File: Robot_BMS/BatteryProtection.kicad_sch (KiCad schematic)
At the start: 18 parts, among them Q10 SIS413DN-T1-GE3, Q11 SIS413DN-T1-GE3, Q12 SIS413DN-T1-GE3, Q13 SIS413DN-T1-GE3, Q14 SIS413DN-T1-GE3, Q15 SIS413DN-T1-GE3, U7 BQ297xy, U8 BQ297xy, U9 BQ297xy

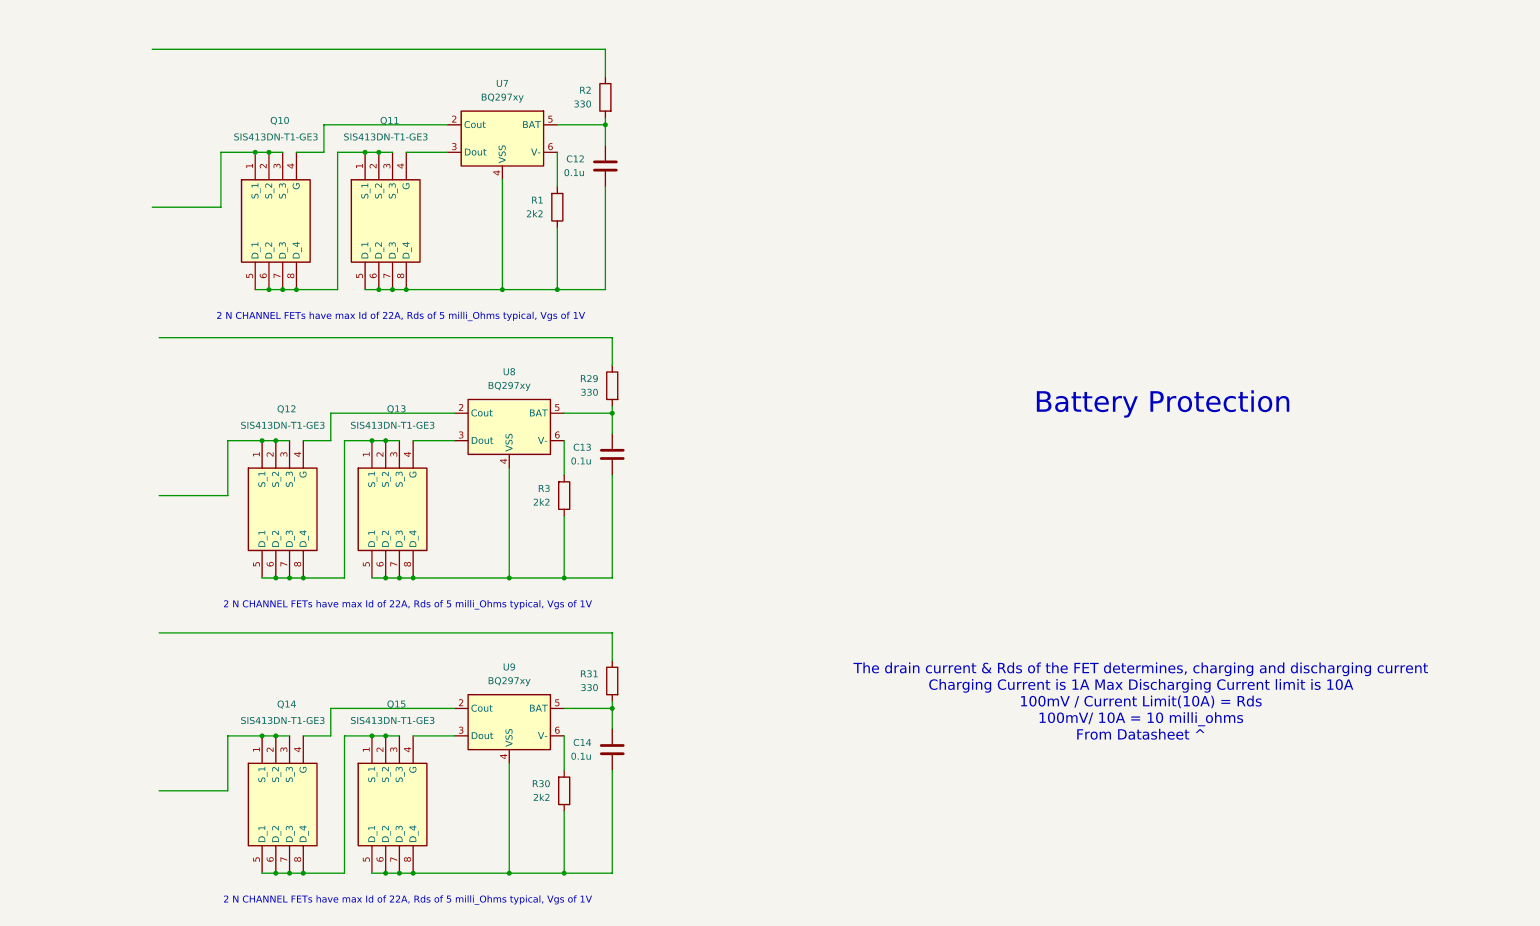
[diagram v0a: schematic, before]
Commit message: cleaning up hierarchical schematics
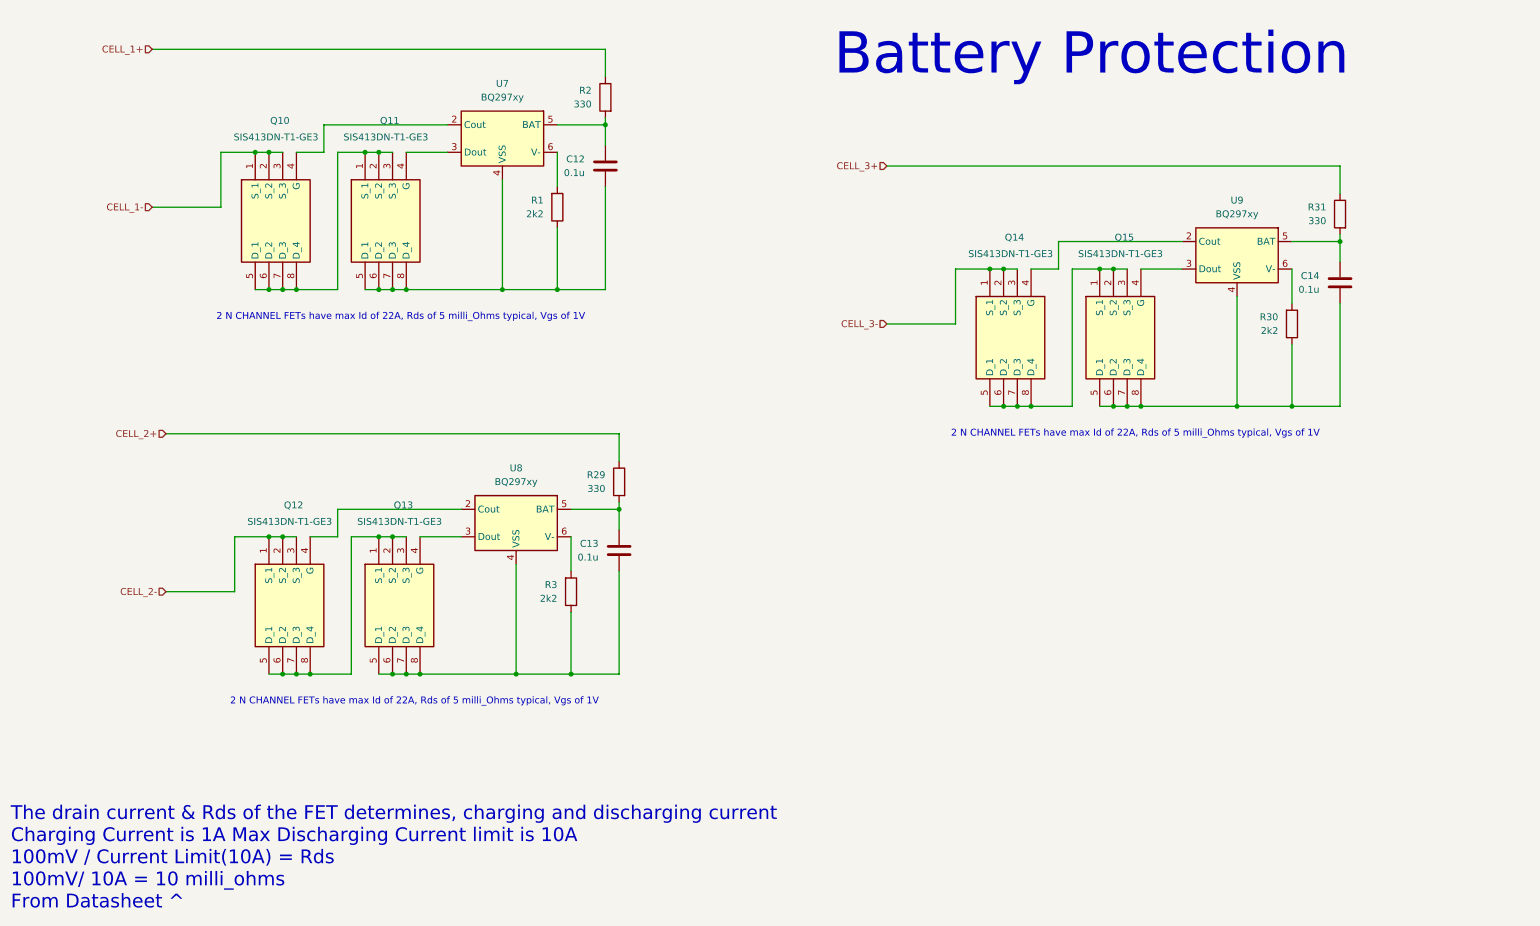
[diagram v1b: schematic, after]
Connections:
- net CELL_1+: now reaches R2.1
- net CELL_3-: now reaches Q14.1 (S_1), Q14.2 (S_2), Q14.3 (S_3)
- net CELL_1-: now reaches Q10.1 (S_1), Q10.2 (S_2), Q10.3 (S_3)
- net CELL_2-: now reaches Q12.1 (S_1), Q12.2 (S_2), Q12.3 (S_3)
- net CELL_2+: now reaches R29.1
- net CELL_3+: now reaches R31.1
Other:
- moved on the sheet: C13, C14, Q12, Q13, Q14, Q15, R29, R3, R30, R31, U8, U9

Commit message: DC power supply added via dc Barrel jack
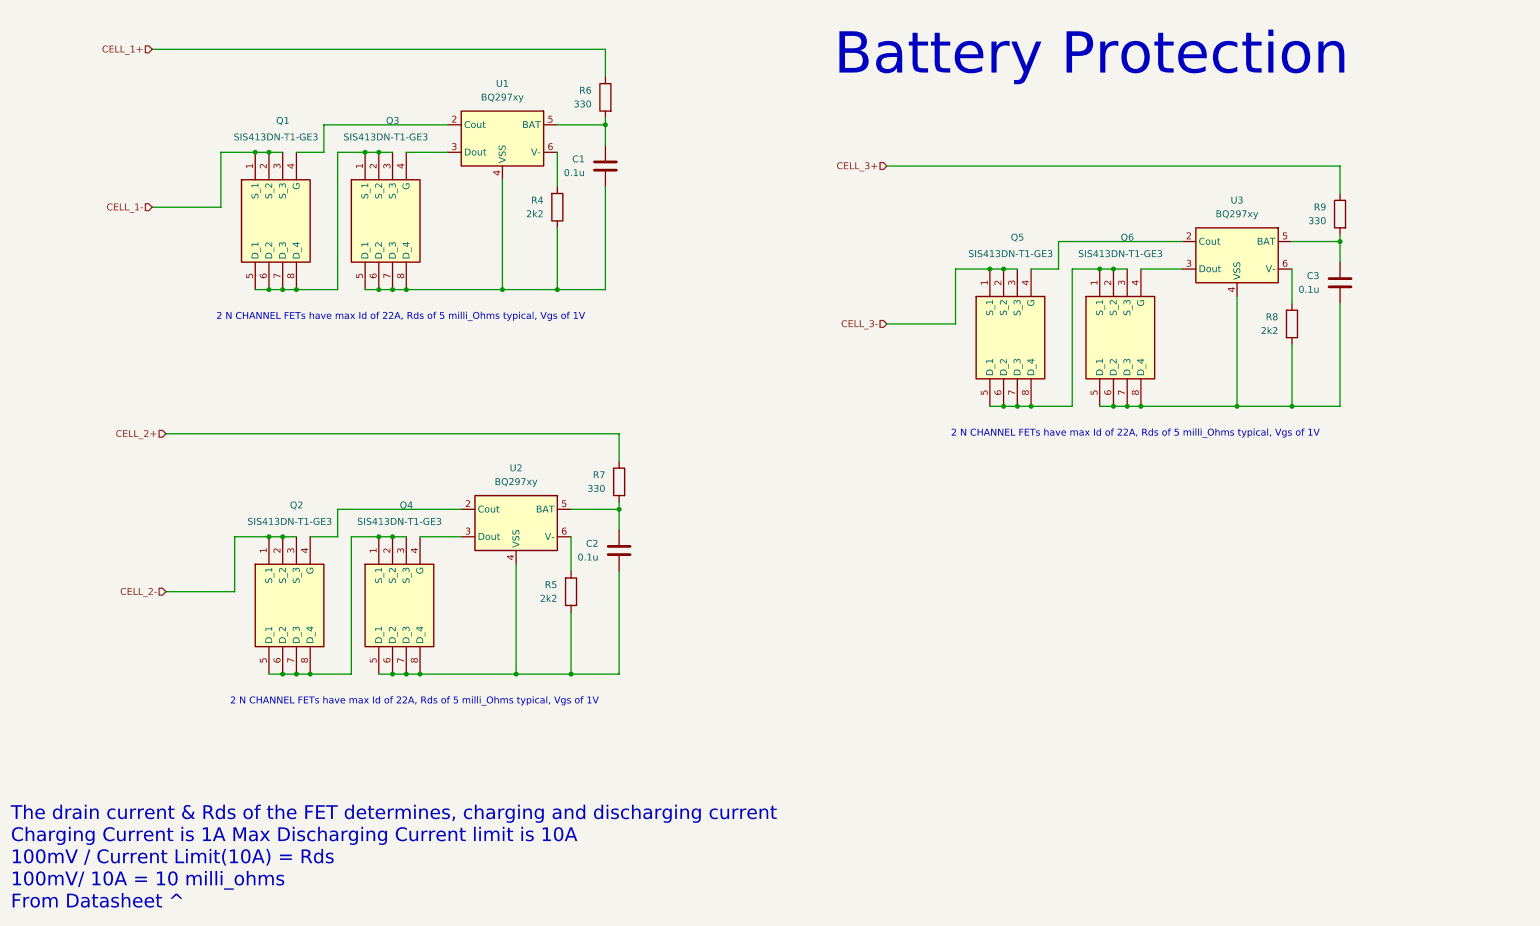
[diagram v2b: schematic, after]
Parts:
- renumbered C12 to C1, C13 to C2, C14 to C3, Q10 to Q1, Q12 to Q2, Q11 to Q3, Q13 to Q4, Q14 to Q5, Q15 to Q6, R1 to R4, R3 to R5, R2 to R6, R29 to R7, R30 to R8, R31 to R9, U7 to U1, U8 to U2, U9 to U3
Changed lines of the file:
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@@
 		(on_board yes)
 		(dnp no)
-		(property "Reference" "Q13"
+		(property "Reference" "Q4"
 			(at 87.63 113.538 90)
 			(effects
@@
 			(project "Robot_BMS"
 				(path "/72551b1c-3d40-4199-8911-e5b015f4abec/ba86123e-f6d5-4f01-be08-e30873977d47"
-					(reference "Q13")
+					(reference "Q4")
 					(unit 1)
 				)
@@
 		(dnp no)
 		(fields_autoplaced yes)
-		(property "Reference" "U9"
+		(property "Reference" "U3"
 			(at 240.03 57.15 0)
 			(effects
@@
 			(project "Robot_BMS"
 				(path "/72551b1c-3d40-4199-8911-e5b015f4abec/ba86123e-f6d5-4f01-be08-e30873977d47"
-					(reference "U9")
+					(reference "U3")
 					(unit 1)
 				)
@@
 		(dnp no)
 		(fields_autoplaced yes)
-		(property "Reference" "R1"
+		(property "Reference" "R4"
 			(at 111.76 57.1499 0)
 			(effects
@@
 			(project "Robot_BMS"
 				(path "/72551b1c-3d40-4199-8911-e5b015f4abec/ba86123e-f6d5-4f01-be08-e30873977d47"
-					(reference "R1")
+					(reference "R4")
 					(unit 1)
 				)
@@
 		(dnp no)
 		(fields_autoplaced yes)
-		(property "Reference" "R2"
+		(property "Reference" "R6"
 			(at 120.65 36.8299 0)
 			(effects
@@
 			(project "Robot_BMS"
 				(path "/72551b1c-3d40-4199-8911-e5b015f4abec/ba86123e-f6d5-4f01-be08-e30873977d47"
-					(reference "R2")
+					(reference "R6")
 					(unit 1)
 				)
@@
 		(on_board yes)
 		(dnp no)
-		(property "Reference" "Q14"
+		(property "Reference" "Q5"
 			(at 200.66 64.008 90)
 			(effects
@@
 			(project "Robot_BMS"
 				(path "/72551b1c-3d40-4199-8911-e5b015f4abec/ba86123e-f6d5-4f01-be08-e30873977d47"
-					(reference "Q14")
+					(reference "Q5")
 					(unit 1)
 				)
@@
 		(on_board yes)
 		(dnp no)
-		(property "Reference" "Q10"
+		(property "Reference" "Q1"
 			(at 64.77 42.418 90)
 			(effects
@@
 			(project "Robot_BMS"
 				(path "/72551b1c-3d40-4199-8911-e5b015f4abec/ba86123e-f6d5-4f01-be08-e30873977d47"
-					(reference "Q10")
+					(reference "Q1")
 					(unit 1)
 				)
@@
 		(dnp no)
 		(fields_autoplaced yes)
-		(property "Reference" "R3"
+		(property "Reference" "R5"
 			(at 114.3 128.2699 0)
 			(effects
@@
 			(project "Robot_BMS"
 				(path "/72551b1c-3d40-4199-8911-e5b015f4abec/ba86123e-f6d5-4f01-be08-e30873977d47"
-					(reference "R3")
+					(reference "R5")
 					(unit 1)
 				)
@@
 		(on_board yes)
 		(dnp no)
-		(property "Reference" "Q15"
+		(property "Reference" "Q6"
 			(at 220.98 64.008 90)
 			(effects
@@
 			(project "Robot_BMS"
 				(path "/72551b1c-3d40-4199-8911-e5b015f4abec/ba86123e-f6d5-4f01-be08-e30873977d47"
-					(reference "Q15")
+					(reference "Q6")
 					(unit 1)
 				)
@@
 		(on_board yes)
 		(dnp no)
-		(property "Reference" "Q12"
+		(property "Reference" "Q2"
 			(at 67.31 113.538 90)
 			(effects
@@
 			(project "Robot_BMS"
 				(path "/72551b1c-3d40-4199-8911-e5b015f4abec/ba86123e-f6d5-4f01-be08-e30873977d47"
-					(reference "Q12")
+					(reference "Q2")
 					(unit 1)
 				)
@@
 		(dnp no)
 		(fields_autoplaced yes)
-		(property "Reference" "R29"
+		(property "Reference" "R7"
 			(at 123.19 107.9499 0)
 			(effects
@@
 			(project "Robot_BMS"
 				(path "/72551b1c-3d40-4199-8911-e5b015f4abec/ba86123e-f6d5-4f01-be08-e30873977d47"
-					(reference "R29")
+					(reference "R7")
 					(unit 1)
 				)
@@
 		(on_board yes)
 		(dnp no)
-		(property "Reference" "Q11"
+		(property "Reference" "Q3"
 			(at 85.09 42.418 90)
 			(effects
@@
 			(project "Robot_BMS"
 				(path "/72551b1c-3d40-4199-8911-e5b015f4abec/ba86123e-f6d5-4f01-be08-e30873977d47"
-					(reference "Q11")
+					(reference "Q3")
 					(unit 1)
 				)
@@
 		(dnp no)
 		(fields_autoplaced yes)
-		(property "Reference" "U8"
+		(property "Reference" "U2"
 			(at 106.68 106.68 0)
 			(effects
@@
 			(project "Robot_BMS"
 				(path "/72551b1c-3d40-4199-8911-e5b015f4abec/ba86123e-f6d5-4f01-be08-e30873977d47"
-					(reference "U8")
+					(reference "U2")
 					(unit 1)
 				)
@@
 		(dnp no)
 		(fields_autoplaced yes)
-		(property "Reference" "R30"
+		(property "Reference" "R8"
 			(at 247.65 78.7399 0)
 			(effects
@@
 			(project "Robot_BMS"
 				(path "/72551b1c-3d40-4199-8911-e5b015f4abec/ba86123e-f6d5-4f01-be08-e30873977d47"
-					(reference "R30")
+					(reference "R8")
 					(unit 1)
 				)
@@
 		(dnp no)
 		(fields_autoplaced yes)
-		(property "Reference" "C14"
+		(property "Reference" "C3"
 			(at 255.27 71.1199 0)
 			(effects
@@
 			(project "Robot_BMS"
 				(path "/72551b1c-3d40-4199-8911-e5b015f4abec/ba86123e-f6d5-4f01-be08-e30873977d47"
-					(reference "C14")
+					(reference "C3")
 					(unit 1)
 				)
@@
 		(dnp no)
 		(fields_autoplaced yes)
-		(property "Reference" "R31"
+		(property "Reference" "R9"
 			(at 256.54 58.4199 0)
 			(effects
@@
 			(project "Robot_BMS"
 				(path "/72551b1c-3d40-4199-8911-e5b015f4abec/ba86123e-f6d5-4f01-be08-e30873977d47"
-					(reference "R31")
+					(reference "R9")
 					(unit 1)
 				)
@@
 		(dnp no)
 		(fields_autoplaced yes)
-		(property "Reference" "U7"
+		(property "Reference" "U1"
 			(at 104.14 35.56 0)
 			(effects
@@
 			(project "Robot_BMS"
 				(path "/72551b1c-3d40-4199-8911-e5b015f4abec/ba86123e-f6d5-4f01-be08-e30873977d47"
-					(reference "U7")
+					(reference "U1")
 					(unit 1)
 				)
@@
 		(dnp no)
 		(fields_autoplaced yes)
-		(property "Reference" "C12"
+		(property "Reference" "C1"
 			(at 119.38 49.5299 0)
 			(effects
@@
 			(project "Robot_BMS"
 				(path "/72551b1c-3d40-4199-8911-e5b015f4abec/ba86123e-f6d5-4f01-be08-e30873977d47"
-					(reference "C12")
+					(reference "C1")
 					(unit 1)
 				)
@@
 		(dnp no)
 		(fields_autoplaced yes)
-		(property "Reference" "C13"
+		(property "Reference" "C2"
 			(at 121.92 120.6499 0)
 			(effects
@@
 			(project "Robot_BMS"
 				(path "/72551b1c-3d40-4199-8911-e5b015f4abec/ba86123e-f6d5-4f01-be08-e30873977d47"
-					(reference "C13")
+					(reference "C2")
 					(unit 1)
 				)
